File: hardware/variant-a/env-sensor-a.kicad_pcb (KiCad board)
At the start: 4 copper layers, 30 x 34 mm, 58 parts, among them J1 USB-C 16P, J2 JST-PH 2P, SW1 SW_PROV, U1 ESP32-C6-MINI-1-N4, U2 SHT45-AD1F, U3 TPS62840DLC, U4 BQ24074RGTR, U5 USBLC6-2SC6

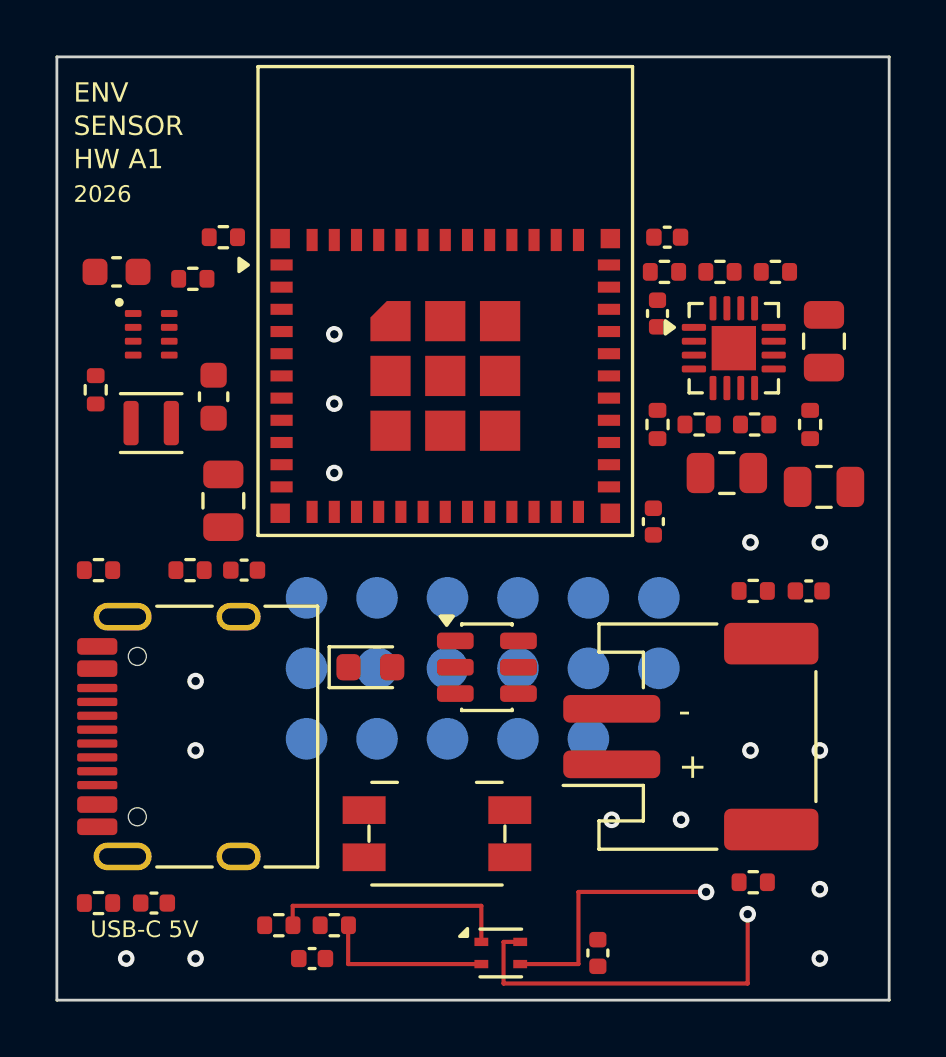
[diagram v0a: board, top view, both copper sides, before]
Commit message: feat(pcb-a,pcb-b): route the boards from the generator, 80 ratsnest down to 58
The next step in the plan was the largest outstanding item: the boards were
placement-complete but unrouted. They are now partially routed, by a maze router
inside the generator rather than by hand.

Why not freerouting: this repository's central claim is that a rule change
regenerates both boards identically. Hand routing, or a one-off Specctra
DSN/SES round trip, breaks exactly that - the next time the neck width moves,
someone has to route both boards again and hope they make the same decisions
twice. So the router lives in tools/boardgen/autoroute.py: Dijkstra on a 0.1 mm
grid over F.Cu and B.Cu against the In1 ground and In2 +3V0 planes, with turn
and via penalties, multi-terminal by repeated multi-source search. No rip-up, no
shoving. It is not a good autorouter; it is a reproducible one, and KiCad's DRC
is the judge.

What it routes: the four sensor-island nets under their own rules, a routed stub
and via into the plane for every +3V0 pad, the ground stitching, and whatever
else it can reach - 38 tracks / 364 mm / 27 vias on A, 35 / 487 mm / 18 on B.
Unconnected goes 80 -> 58 on both boards with zero DRC errors.

Five real defects surfaced on the way, all fixed at source:

- Blocking rectangles were rounded outward by `int(x)+2`, a fifth of a
  millimetre, which is exactly enough to seal every pad on a 0.5 mm-pitch part
  and make the charger, the regulator and the USB-C receptacle unroutable. The
  same bug was latent in the island router.
- Clearance was modelled as one worst-case number. At 0.22 mm the blocking band
  around a 0.5 mm-pitch pad is 0.52 mm - it seals the pad's own escape corridor.
  Clearance is now per net class, as KiCad actually applies it.
- Placement that only avoids courtyard overlap is not routable placement.
  Passives packed at the 0.1 mm minimum around an IC satisfy DRC and then seal
  every escape corridor, which the router discovers much later and much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
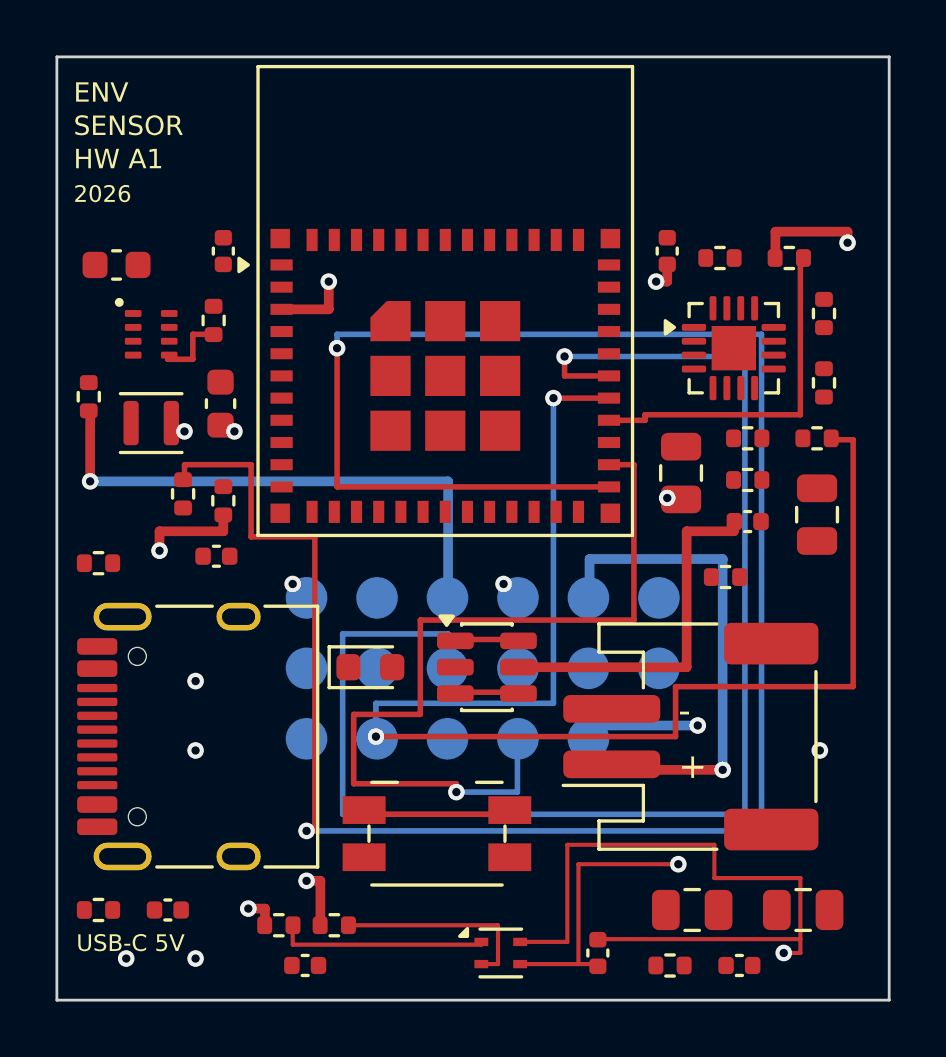
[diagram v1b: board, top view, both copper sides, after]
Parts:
- moved C4 19.9 mm to (105.8, 78.0)
- moved C1 16.5 mm to (122.5, 75.0)
- moved C10 15.8 mm to (122.9, 90.8)
- moved C11 15.3 mm to (126.9, 90.8)
- moved C13 13.7 mm to (124.6, 92.8)
- moved C2 11.5 mm to (106.0, 67.0), turned to 90 degrees
- moved C3 9.76 mm to (122.0, 67.0)
- moved R1 9.50 mm to (106.0, 76.0), turned to 90 degrees
- moved C12 8.17 mm to (124.9, 76.8), turned to 0 degrees
- moved R10 6.95 mm to (127.4, 73.8)
- moved R9 6.82 mm to (126.4, 67.2)
- moved R8 6.71 mm to (124.9, 73.8)
- moved R7 6.41 mm to (123.9, 67.2), turned to 0 degrees
- moved C9 6.25 mm to (127.4, 76.5)
- moved R11 4.72 mm to (127.7, 69.2), turned to 90 degrees
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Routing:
- net LED_N: track 0.00 -> 83.6 mm, vias 0 -> 2
- net UART_RX: track 0.00 -> 51.3 mm, vias 0 -> 1
- net CHG_N: track 0.00 -> 49.4 mm, vias 0 -> 2
- net TEST_MODE: track 0.00 -> 30.6 mm, vias 0 -> 1
- net VSYS: track 0.00 -> 19.7 mm, vias 0 -> 1
- net +3V0: track 9.30 -> 27.6 mm, vias 1 -> 11
- net VBAT: track 0.00 -> 18.0 mm, vias 0 -> 1
- net GND: track 13.4 -> 30.8 mm, vias 16 -> 8
- net VBUS: track 0.00 -> 13.0 mm
- net PG_N: track 0.00 -> 12.9 mm
- net BTN_PROV: track 0.00 -> 5.60 mm
- net VSET: track 0.00 -> 2.60 mm
- net USB_DP: track 0.00 -> 2.20 mm
- net USB_DM: track 0.00 -> 2.20 mm
- net SDA: track 8.80 -> 7.60 mm
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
